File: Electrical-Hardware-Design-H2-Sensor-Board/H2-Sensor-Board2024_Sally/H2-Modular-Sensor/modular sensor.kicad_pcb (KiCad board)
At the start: 2 copper layers, 60 x 30 mm, 15 parts, among them J1 Molex_6_Pin, U1 AZ1117IH-5.0, U2 MCP6007

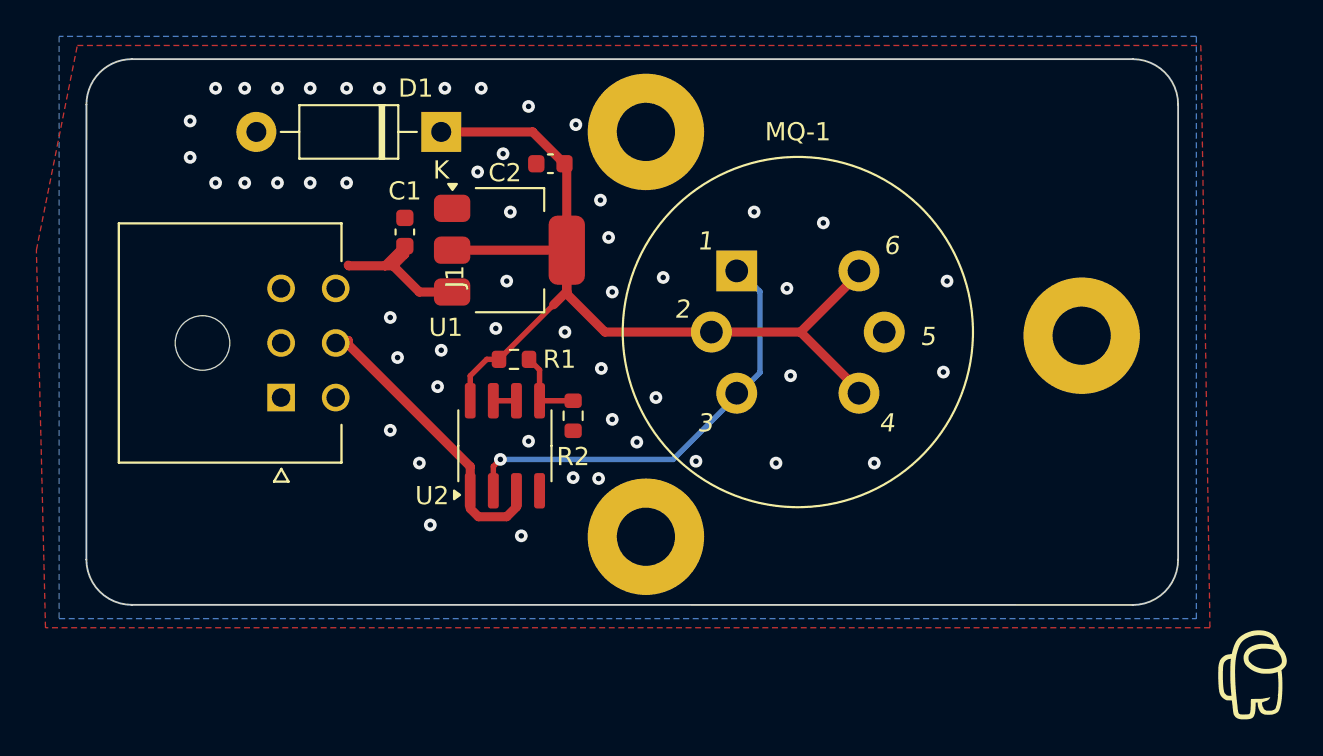
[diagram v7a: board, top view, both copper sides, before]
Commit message: MoSen gerber generated
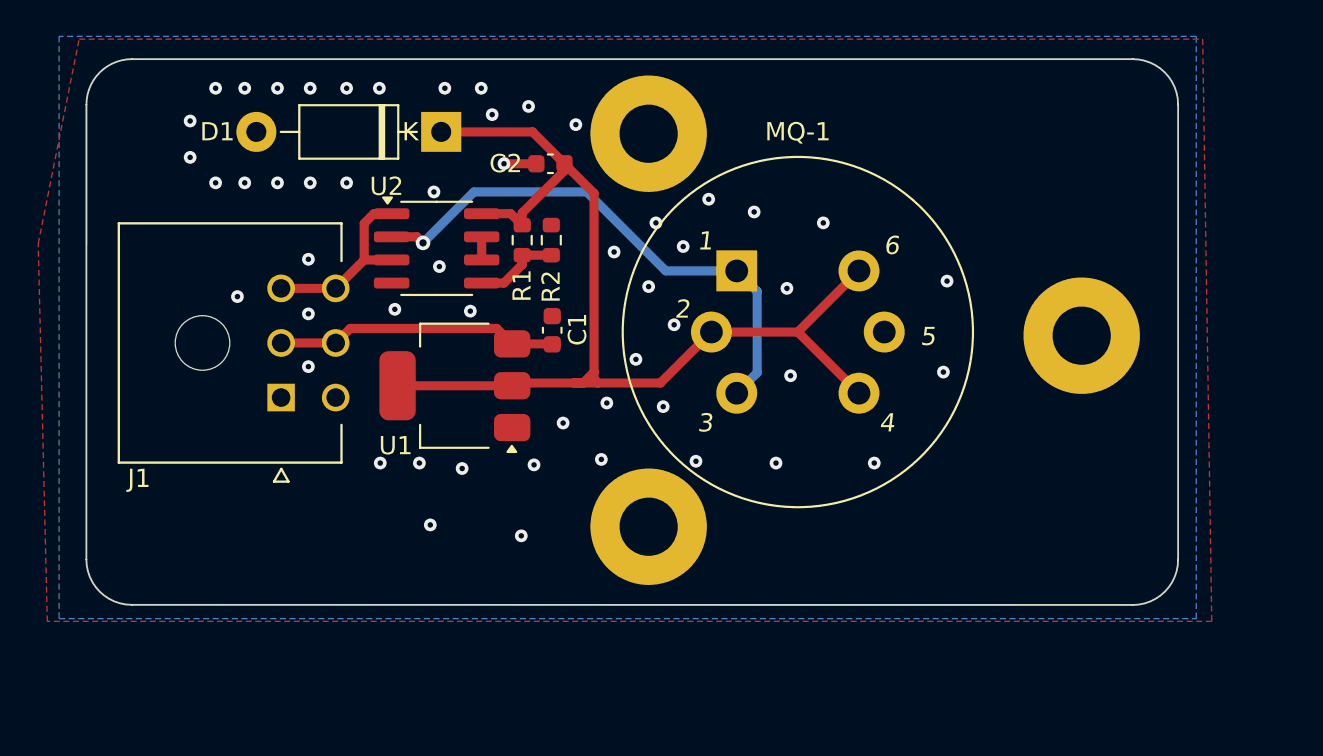
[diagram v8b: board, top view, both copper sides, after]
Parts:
- removed the G*** at (172.6, 90.3)
- added kibuzzard-67B982E7: G***, kibuzzard-67B982E7, B.Cu at (160.4, 83.6)
- added kibuzzard-67B98323: G***, kibuzzard-67B98323, B.Cu at (150.0, 83.6)
- added kibuzzard-67B98359: G***, kibuzzard-67B98359, B.Cu at (159.0, 62.4)
- moved U2 11.5 mm to (127.8, 66.9), turned to 0 degrees
- moved C1 9.73 mm to (134.1, 71.4)
- moved R2 9.72 mm to (134.1, 66.5), turned to -90 degrees
- moved U1 8.03 mm to (128.8, 74.5), turned to 180 degrees
- moved R1 6.57 mm to (132.4, 66.5), turned to 90 degrees
- moved H2 0.57 mm to (139.4, 82.2)
- moved H3 0.18 mm to (139.4, 60.6)
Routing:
- net /H2_PWR_unfilter: track 9.21 -> 15.6 mm
- net /V_Heater: track 55.0 -> 61.1 mm
- net /V_Sensed: track 16.4 -> 10.5 mm
- net /V_RL: track 24.2 -> 29.7 mm
- net GND: track 0.00 -> 1.99 mm, vias 51 -> 53
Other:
- board text removed: "H2 MoSen R${REVISION}"
- board text removed: "Owen W. || 01.25 || Sally"
